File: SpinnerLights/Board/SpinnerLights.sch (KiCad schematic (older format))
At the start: 17 parts, among them U1 SeeeduinoXIAO, U2 ADXL343

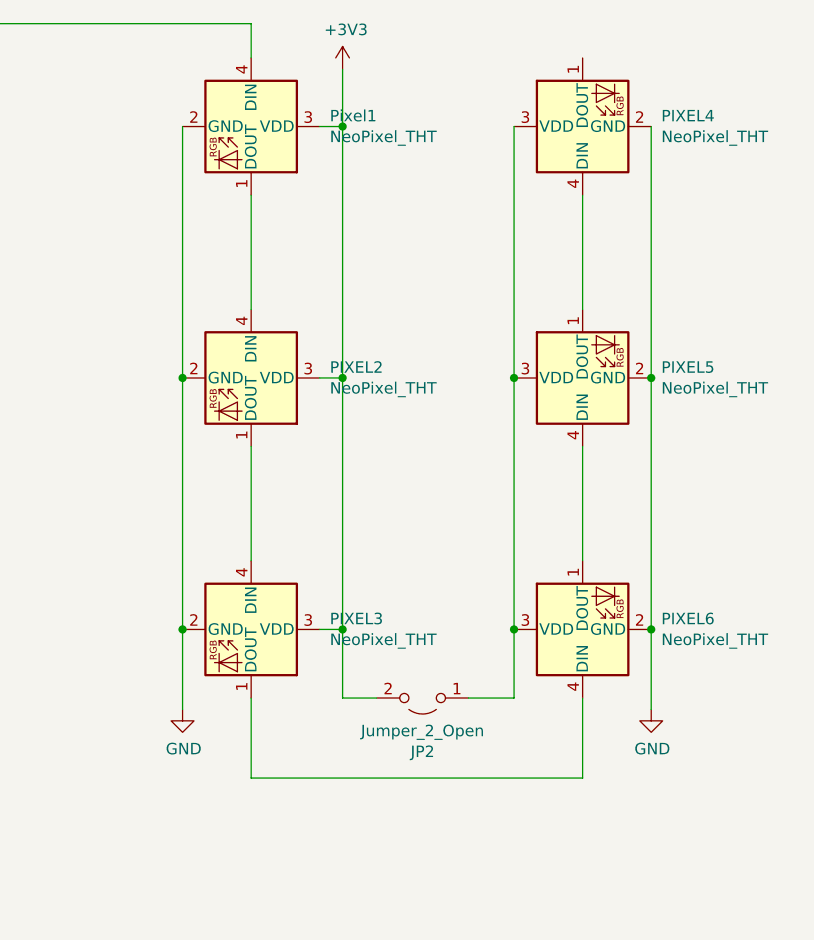
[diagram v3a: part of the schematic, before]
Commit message: SpinnerLights: More progress on board layout
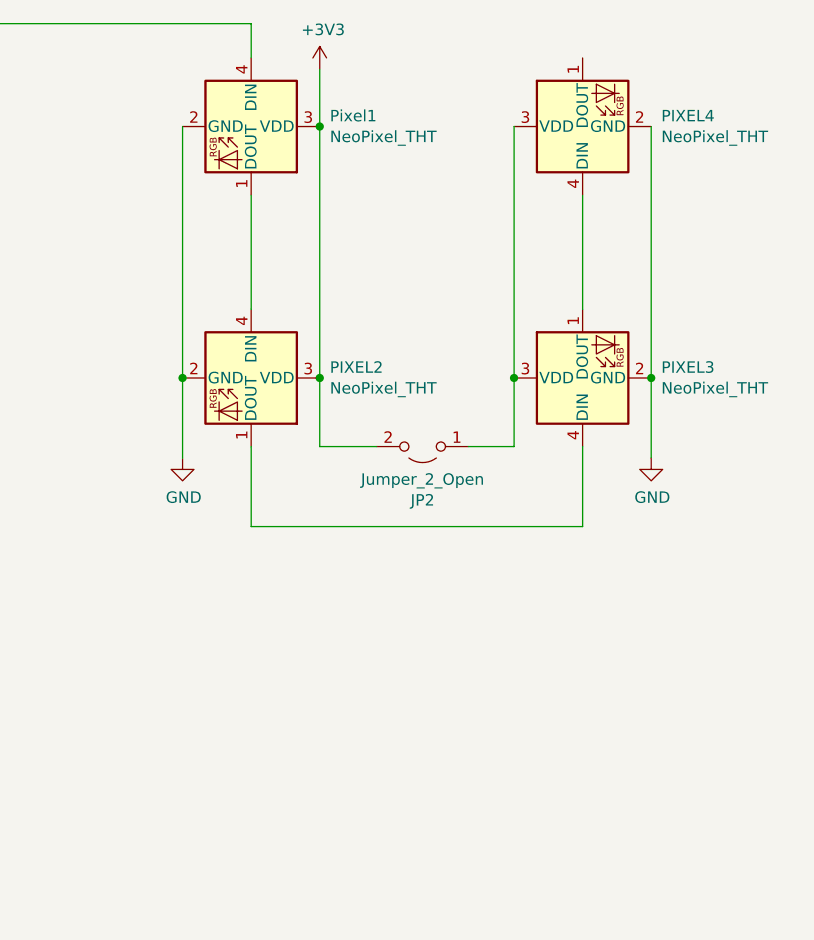
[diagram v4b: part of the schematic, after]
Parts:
- removed PIXEL4, PIXEL5: NeoPixel_THT, LED_SMD:LED_SK6812MINI_PLCC4_3.5x3.5mm_P1.75mm, symbol LED:NeoPixel_THT
- renumbered PIXEL6 to PIXEL4
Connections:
- net +3V3: no longer PIXEL3.3 (VDD)
- net at JP2.1 (A), PIXEL4.3 (VDD): now also PIXEL3.3 (VDD)
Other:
- moved on the sheet: JP2, PIXEL4
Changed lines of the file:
@@
 L power:+3V3 #PWR011
 U 1 1 616A7416
-P 9300 1350
-F 0 "#PWR011" H 9300 1200 50  0001 C CNN
-F 1 "+3V3" H 9315 1523 50  0000 C CNN
-F 2 "" H 9300 1350 50  0001 C CNN
-F 3 "" H 9300 1350 50  0001 C CNN
-	1    9300 1350
+P 9200 1350
+F 0 "#PWR011" H 9200 1200 50  0001 C CNN
+F 1 "+3V3" H 9215 1523 50  0000 C CNN
+F 2 "" H 9200 1350 50  0001 C CNN
+F 3 "" H 9200 1350 50  0001 C CNN
+	1    9200 1350
 	1    0    0    -1
 $EndComp
 Wire Wire Line
-	9200 1600 9300 1600
-$Comp
-L LED:NeoPixel_THT PIXEL2
-U 1 1 616B291A
-P 8900 2700
-F 0 "PIXEL2" V 8854 3044 50  0000 L CNN
-F 1 "NeoPixel_THT" V 8945 3044 50  0000 L CNN
-F 2 "LED_SMD:LED_SK6812MINI_PLCC4_3.5x3.5mm_P1.75mm" H 8950 2400 50  0001 L TNN
-F 3 "https://www.adafruit.com/product/1938" H 9000 2325 50  0001 L TNN
-	1    8900 2700
-	0    1    1    0
-$EndComp
-Wire Wire Line
-	9200 2700 9300 2700
-$Comp
-L LED:NeoPixel_THT PIXEL3
-U 1 1 616B438B
-P 8900 3800
-F 0 "PIXEL3" V 8854 4144 50  0000 L CNN
-F 1 "NeoPixel_THT" V 8945 4144 50  0000 L CNN
-F 2 "LED_SMD:LED_SK6812MINI_PLCC4_3.5x3.5mm_P1.75mm" H 8950 3500 50  0001 L TNN
-F 3 "https://www.adafruit.com/product/1938" H 9000 3425 50  0001 L TNN
-	1    8900 3800
-	0    1    1    0
-$EndComp
-Wire Wire Line
-	9200 3800 9300 3800
-Wire Wire Line
 	5100 1150 8900 1150
-Wire Wire Line
-	8900 3000 8900 3500
-Wire Wire Line
-	8900 2400 8900 1900
-$Comp
-L LED:NeoPixel_THT PIXEL6
-U 1 1 616C9B9C
-P 10350 3800
-F 0 "PIXEL6" V 10396 3456 50  0000 R CNN
-F 1 "NeoPixel_THT" V 10305 3456 50  0000 R CNN
-F 2 "LED_SMD:LED_SK6812MINI_PLCC4_3.5x3.5mm_P1.75mm" H 10400 3500 50  0001 L TNN
-F 3 "https://www.adafruit.com/product/1938" H 10450 3425 50  0001 L TNN
-	1    10350 3800
-	0    -1   -1   0
-$EndComp
-$Comp
-L LED:NeoPixel_THT PIXEL5
-U 1 1 616C9BB0
-P 10350 2700
-F 0 "PIXEL5" V 10396 2356 50  0000 R CNN
-F 1 "NeoPixel_THT" V 10305 2356 50  0000 R CNN
-F 2 "LED_SMD:LED_SK6812MINI_PLCC4_3.5x3.5mm_P1.75mm" H 10400 2400 50  0001 L TNN
-F 3 "https://www.adafruit.com/product/1938" H 10450 2325 50  0001 L TNN
-	1    10350 2700
-	0    -1   -1   0
-$EndComp
 $Comp
 L LED:NeoPixel_THT PIXEL4
-U 1 1 616C9BC4
+U 1 1 616C9B9C
 P 10350 1600
 F 0 "PIXEL4" V 10396 1256 50  0000 R CNN
@@
 	0    -1   -1   0
 $EndComp
-Wire Wire Line
-	10350 2400 10350 1900
-Wire Wire Line
-	10350 3000 10350 3500
 $Comp
 L Jumper:Jumper_2_Open JP2
 U 1 1 616CB68A
-P 9650 4100
-F 0 "JP2" H 9650 4335 50  0000 C CNN
-F 1 "Jumper_2_Open" H 9650 4244 50  0000 C CNN
-F 2 "Jumper:SolderJumper-2_P1.3mm_Open_RoundedPad1.0x1.5mm" H 9650 4100 50  0001 C CNN
-F 3 "~" H 9650 4100 50  0001 C CNN
-	1    9650 4100
+P 9650 3000
+F 0 "JP2" H 9650 3235 50  0000 C CNN
+F 1 "Jumper_2_Open" H 9650 3144 50  0000 C CNN
+F 2 "Jumper:SolderJumper-2_P1.3mm_Open_RoundedPad1.0x1.5mm" H 9650 3000 50  0001 C CNN
+F 3 "~" H 9650 3000 50  0001 C CNN
+	1    9650 3000
 	-1   0    0    1
 $EndComp
 Wire Wire Line
-	9300 1350 9300 1600
+	9850 3000 10050 3000
 Wire Wire Line
-	9300 1600 9300 2700
-Connection ~ 9300 1600
+	10350 3000 10350 3350
 Wire Wire Line
-	9300 2700 9300 3800
-Connection ~ 9300 2700
+	10350 3350 8900 3350
 Wire Wire Line
-	9300 3800 9300 4100
-Wire Wire Line
-	9300 4100 9450 4100
-Connection ~ 9300 3800
-Wire Wire Line
-	9850 4100 10050 4100
-Wire Wire Line
-	10050 4100 10050 3800
-Wire Wire Line
-	10050 3800 10050 2700
-Connection ~ 10050 3800
-Wire Wire Line
-	10050 1600 10050 2700
-Connection ~ 10050 2700
-Wire Wire Line
-	10350 4100 10350 4450
-Wire Wire Line
-	10350 4450 8900 4450
-Wire Wire Line
-	8900 4450 8900 4100
+	8900 3350 8900 3000
 Wire Wire Line
 	5100 1150 5100 3100
@@
 L power:GND #PWR014
 U 1 1 616C9BA8
-P 10650 4150
-F 0 "#PWR014" H 10650 3900 50  0001 C CNN
-F 1 "GND" H 10655 3977 50  0000 C CNN
-F 2 "" H 10650 4150 50  0001 C CNN
-F 3 "" H 10650 4150 50  0001 C CNN
-	1    10650 4150
+P 10650 3050
+F 0 "#PWR014" H 10650 2800 50  0001 C CNN
+F 1 "GND" H 10655 2877 50  0000 C CNN
+F 2 "" H 10650 3050 50  0001 C CNN
+F 3 "" H 10650 3050 50  0001 C CNN
+	1    10650 3050
 	1    0    0    -1
 $EndComp
-Wire Wire Line
-	10650 1600 10650 2700
-Wire Wire Line
-	10650 2700 10650 3800
-Connection ~ 10650 2700
-Wire Wire Line
-	10650 3800 10650 4150
-Connection ~ 10650 3800
 $Comp
 L power:GND #PWR0101
 U 1 1 616F33F2
-P 8600 4150
-F 0 "#PWR0101" H 8600 3900 50  0001 C CNN
-F 1 "GND" H 8605 3977 50  0000 C CNN
-F 2 "" H 8600 4150 50  0001 C CNN
-F 3 "" H 8600 4150 50  0001 C CNN
-	1    8600 4150
+P 8600 3050
+F 0 "#PWR0101" H 8600 2800 50  0001 C CNN
+F 1 "GND" H 8605 2877 50  0000 C CNN
+F 2 "" H 8600 3050 50  0001 C CNN
+F 3 "" H 8600 3050 50  0001 C CNN
+	1    8600 3050
 	1    0    0    -1
 $EndComp
-Wire Wire Line
-	8600 4150 8600 3800
-Wire Wire Line
-	8600 3800 8600 2700
-Connection ~ 8600 3800
-Wire Wire Line
-	8600 2700 8600 1600
-Connection ~ 8600 2700
 $Comp
 L BAT-HLD-001-THM:BAT-HLD-001-THM BT2
@@
 Wire Wire Line
 	5400 4800 6200 4800
+Wire Wire Line
+	8900 2400 8900 1900
+Wire Wire Line
+	8600 2700 8600 1600
+Connection ~ 8600 2700
+$Comp
+L LED:NeoPixel_THT PIXEL2
+U 1 1 616B291A
+P 8900 2700
+F 0 "PIXEL2" V 8854 3044 50  0000 L CNN
+F 1 "NeoPixel_THT" V 8945 3044 50  0000 L CNN
+F 2 "LED_SMD:LED_SK6812MINI_PLCC4_3.5x3.5mm_P1.75mm" H 8950 2400 50  0001 L TNN
+F 3 "https://www.adafruit.com/product/1938" H 9000 2325 50  0001 L TNN
+	1    8900 2700
+	0    1    1    0
+$EndComp
+Wire Wire Line
+	8600 2700 8600 3050
+Wire Wire Line
+	9200 1350 9200 1600
+Wire Wire Line
+	9200 1600 9200 2700
+Connection ~ 9200 1600
+Wire Wire Line
+	9200 2700 9200 3000
+Wire Wire Line
+	9200 3000 9450 3000
+Connection ~ 9200 2700
+Wire Wire Line
+	10050 1600 10050 2700
+Wire Wire Line
+	10650 1600 10650 2700
+$Comp
+L LED:NeoPixel_THT PIXEL3
+U 1 1 6175018F
+P 10350 2700
+F 0 "PIXEL3" V 10396 2356 50  0000 R CNN
+F 1 "NeoPixel_THT" V 10305 2356 50  0000 R CNN
+F 2 "LED_SMD:LED_SK6812MINI_PLCC4_3.5x3.5mm_P1.75mm" H 10400 2400 50  0001 L TNN
+F 3 "https://www.adafruit.com/product/1938" H 10450 2325 50  0001 L TNN
+	1    10350 2700
+	0    -1   -1   0
+$EndComp
+Connection ~ 10650 2700
+Wire Wire Line
+	10650 2700 10650 3050
+Connection ~ 10050 2700
+Wire Wire Line
+	10050 2700 10050 3000
+Wire Wire Line
+	10350 2400 10350 1900
 $EndSCHEMATC

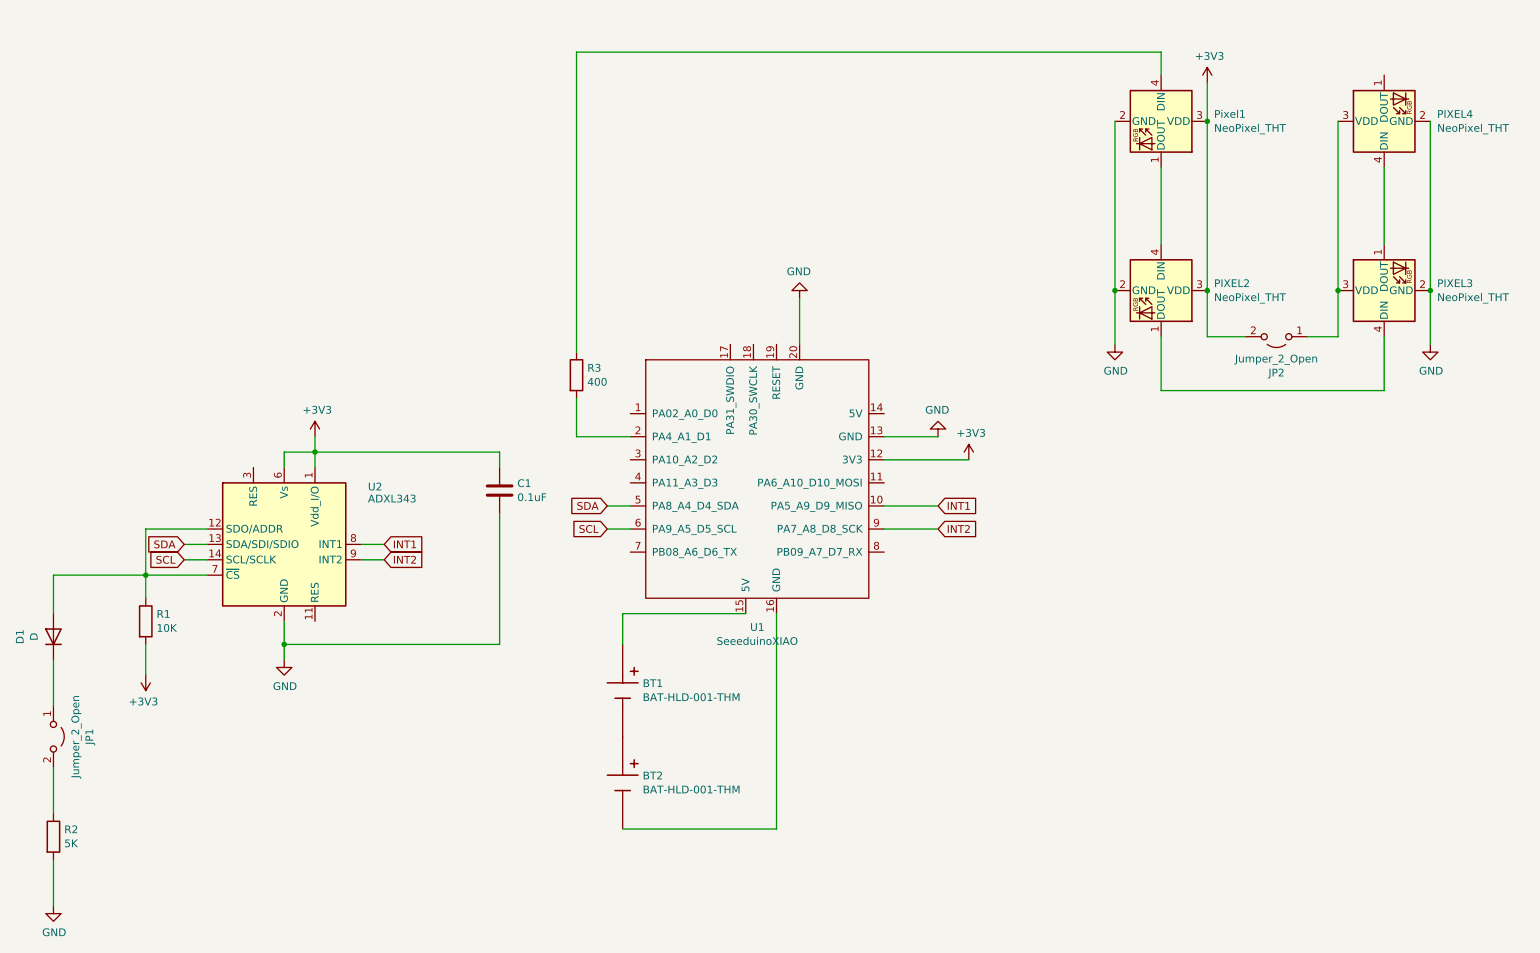
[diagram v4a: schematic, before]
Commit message: SpinnerLights: started laying down wires
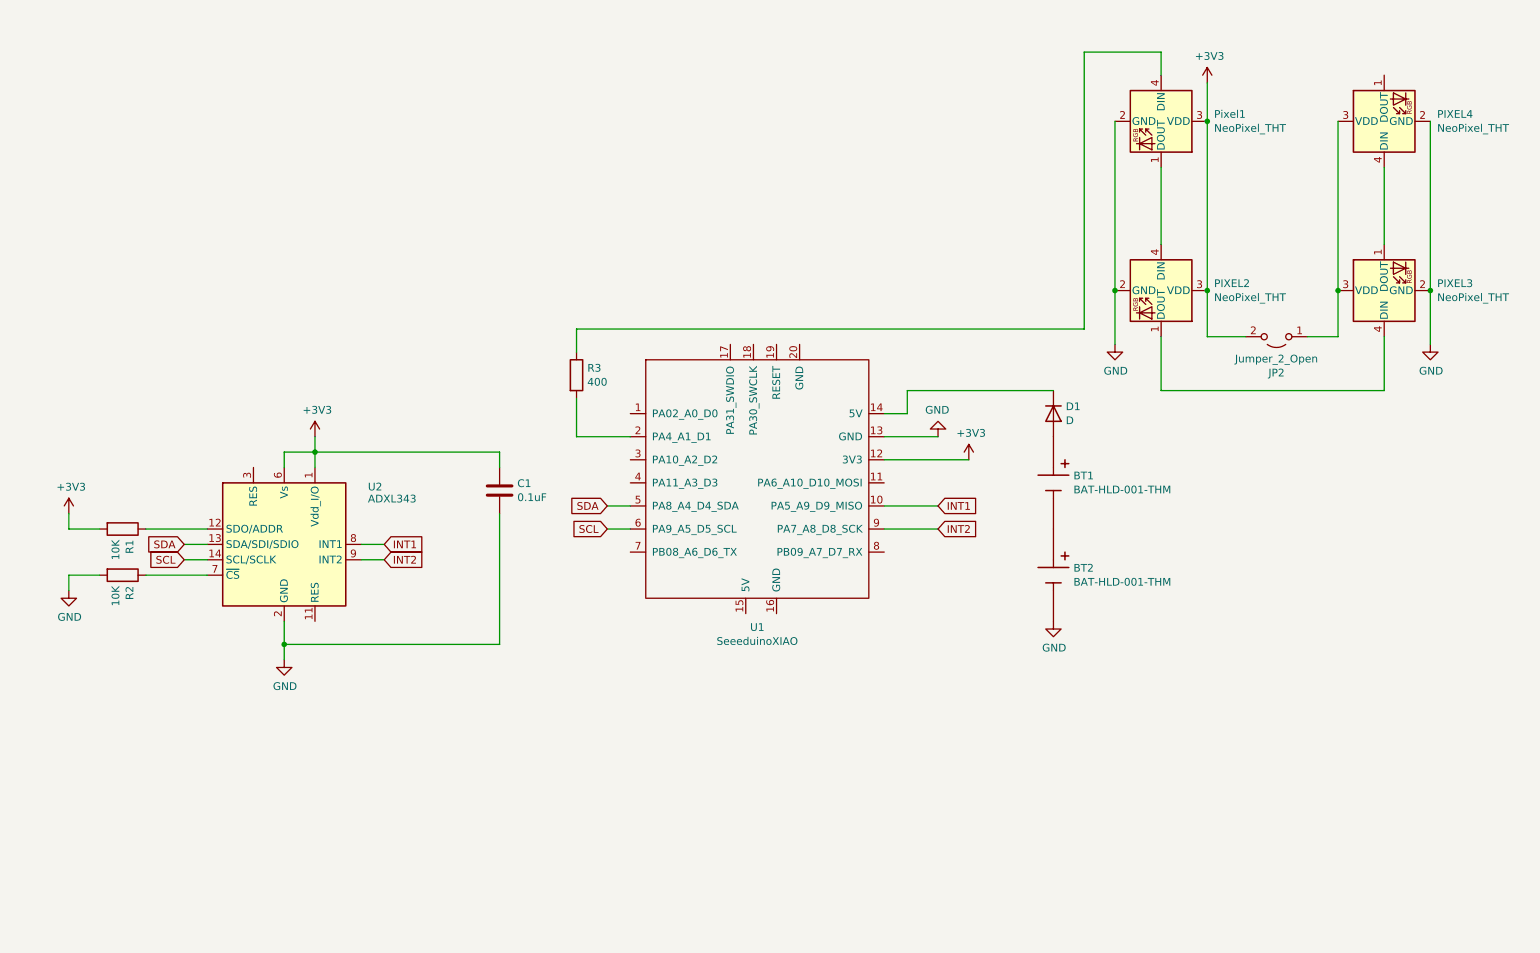
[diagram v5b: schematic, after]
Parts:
- removed JP1: Jumper_2_Open, Jumper:SolderJumper-2_P1.3mm_Open_RoundedPad1.0x1.5mm, symbol Jumper:Jumper_2_Open
- BT1, BT2: footprint BAT_BAT-HLD-001-THM -> BAT-HLD-001-THM:BAT_BAT-HLD-001-THM
- D1: footprint Diode_SMD:D_0603_1608Metric_Pad1.05x0.95mm_HandSolder -> Diode_SMD:D_SOD-323
- R2: value 5K -> 10K
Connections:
- net GND: now also BT2.N; no longer U1.20 (GND)
- net at U1.14 (5V): now also D1.1 (K)
- net at BT1.P1, BT1.P2, BT1.P3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: now also D1.2 (A); no longer U1.15 (5V)
- net at U1.16 (GND): no longer BT2.N
- net at R1.1, U2.12 (SDO/ADDR): no longer D1.2 (A), U2.7 (~CS)
- net at R2.1: now also U2.7 (~CS)
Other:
- moved on the sheet: BT1, BT2, R1

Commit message: SpinnerLights: Almost complete routing
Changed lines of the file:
@@
 $EndComp
-Wire Wire Line
-	9850 3000 10050 3000
 Wire Wire Line
 	10350 3000 10350 3350
@@
 Connection ~ 9200 2700
 Wire Wire Line
-	10050 1600 10050 2700
-Wire Wire Line
-	10650 1600 10650 2700
-$Comp
-L LED:NeoPixel_THT PIXEL3
-U 1 1 6175018F
-P 10350 2700
-F 0 "PIXEL3" V 10396 2356 50  0000 R CNN
-F 1 "NeoPixel_THT" V 10305 2356 50  0000 R CNN
-F 2 "LED_SMD:LED_SK6812MINI_PLCC4_3.5x3.5mm_P1.75mm" H 10400 2400 50  0001 L TNN
-F 3 "https://www.adafruit.com/product/1938" H 10450 2325 50  0001 L TNN
-	1    10350 2700
-	0    -1   -1   0
-$EndComp
-Connection ~ 10650 2700
-Wire Wire Line
-	10650 2700 10650 3050
-Connection ~ 10050 2700
-Wire Wire Line
-	10050 2700 10050 3000
-Wire Wire Line
 	10350 2400 10350 1900
 $Comp
@@
 $EndComp
 Wire Wire Line
-	5100 3100 5100 2950
-Wire Wire Line
-	5100 2950 8400 2950
-Wire Wire Line
-	8400 2950 8400 1150
-Wire Wire Line
-	8400 1150 8900 1150
-Wire Wire Line
 	1800 4550 1800 4650
 Wire Wire Line
@@
 	1    0    0    -1
 $EndComp
+Wire Wire Line
+	5100 3100 5100 2950
+Wire Wire Line
+	5100 2950 8400 2950
+Wire Wire Line
+	8400 2950 8400 1150
+Wire Wire Line
+	8400 1150 8900 1150
+Wire Wire Line
+	10050 2700 10050 3000
+Wire Wire Line
+	10050 1600 10050 2700
+Connection ~ 10050 2700
+Wire Wire Line
+	10650 2700 10650 3050
+Wire Wire Line
+	10650 1600 10650 2700
+Connection ~ 10650 2700
+$Comp
+L LED:NeoPixel_THT PIXEL3
+U 1 1 6175018F
+P 10350 2700
+F 0 "PIXEL3" V 10396 2356 50  0000 R CNN
+F 1 "NeoPixel_THT" V 10305 2356 50  0000 R CNN
+F 2 "LED_SMD:LED_SK6812MINI_PLCC4_3.5x3.5mm_P1.75mm" H 10400 2400 50  0001 L TNN
+F 3 "https://www.adafruit.com/product/1938" H 10450 2325 50  0001 L TNN
+	1    10350 2700
+	0    -1   -1   0
+$EndComp
+Wire Wire Line
+	10050 3000 9850 3000
 $EndSCHEMATC
